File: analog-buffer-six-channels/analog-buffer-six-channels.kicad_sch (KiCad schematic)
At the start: 8 parts, among them J1 Conn_02x10_Odd_Even, J2 Conn_02x08_Odd_Even

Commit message: Generated gerber files for analog-buffer board
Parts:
- added R14: DNP, Resistor_SMD:R_0805_2012Metric, symbol Device:R_Small
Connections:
- net -VCC: now also R14.1
- net GND: now also R14.2
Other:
- note added: "[1]"
- note added: "[1] Place this resistor if single supply operation is intended. Please note that if this resistor is placed, -Vcc and GND will be shorted. Thus, it must be ensured that no active supply is present on the -Vcc rail."
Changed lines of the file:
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@@
+    (stroke (width 0) (type default) (color 0 0 0 0))
+  )
+  (wire (pts (xy 67.056 64.77) (xy 69.596 64.77))
     (stroke (width 0) (type default) (color 0 0 0 0))
   )
@@
     (stroke (width 0) (type default) (color 0 0 0 0))
   )
+  (wire (pts (xy 74.676 64.77) (xy 77.216 64.77))
+    (stroke (width 0) (type default) (color 0 0 0 0))
+  )
   (wire (pts (xy 187.579 24.892) (xy 189.484 24.892))
     (stroke (width 0) (type default) (color 0 0 0 0))
@@
   (wire (pts (xy 236.093 33.401) (xy 236.093 35.941))
     (stroke (width 0) (type default) (color 0 0 0 0))
+  )
+  (text "[1]" (at 70.485 69.977 0)
+    (effects (font (size 1.27 1.27)) (justify left bottom))
+  )
+  (text "[1] Place this resistor if single supply operation is \nintended. Please note that if this resistor is placed,\n-Vcc and GND will be shorted. Thus, it must be ensured \nthat no active  supply is present on the -Vcc rail. "
+    (at 25.654 120.65 0)
+    (effects (font (size 1.27 1.27)) (justify left bottom))
   )
   (label "S4o" (at 169.291 29.972 0)
@@
     )
     (property "Datasheet" "" (id 3) (at 248.793 41.275 0)
+      (effects (font (size 1.27 1.27)) hide)
+    )
+    (pin "1")
+  )
+  (symbol (lib_id "CL_power:-VCC") (at 67.056 64.77 0) (unit 1)
+    (in_bom yes) (on_board yes)
+    (property "Reference" "#PWR030" (id 0) (at 67.056 68.58 0)
+      (effects (font (size 1.27 1.27)) hide)
+    )
+    (property "Value" "-VCC" (id 1) (at 67.056 60.96 0))
+    (property "Footprint" "" (id 2) (at 67.056 64.77 0)
+      (effects (font (size 1.27 1.27)) hide)
+    )
+    (property "Datasheet" "" (id 3) (at 67.056 64.77 0)
       (effects (font (size 1.27 1.27)) hide)
     )
@@
     (pin "9")
   )
+  (symbol (lib_id "power:GND") (at 77.216 64.77 180) (unit 1)
+    (in_bom yes) (on_board yes)
+    (property "Reference" "#PWR031" (id 0) (at 77.216 58.42 0)
+      (effects (font (size 1.27 1.27)) hide)
+    )
+    (property "Value" "GND" (id 1) (at 77.216 60.96 0))
+    (property "Footprint" "" (id 2) (at 77.216 64.77 0)
+      (effects (font (size 1.27 1.27)) hide)
+    )
+    (property "Datasheet" "" (id 3) (at 77.216 64.77 0)
+      (effects (font (size 1.27 1.27)) hide)
+    )
+    (pin "1")
+  )
   (symbol (lib_id "CL_power:-VCC") (at 187.579 35.052 180) (unit 1)
     (in_bom yes) (on_board yes)
@@
     )
     (property "Datasheet" "~" (id 3) (at 94.361 29.591 0)
+      (effects (font (size 1.27 1.27)) hide)
+    )
+    (pin "1")
+    (pin "2")
+  )
+  (symbol (lib_id "Device:R_Small") (at 72.136 64.77 90) (unit 1)
+    (in_bom yes) (on_board yes)
+    (property "Reference" "R14" (id 0) (at 74.041 62.992 90)
+      (effects (font (size 1.27 1.27)) (justify left))
+    )
+    (property "Value" "DNP" (id 1) (at 74.168 66.548 90)
+      (effects (font (size 1.27 1.27)) (justify left))
+    )
+    (property "Footprint" "Resistor_SMD:R_0805_2012Metric" (id 2) (at 72.136 64.77 0)
+      (effects (font (size 1.27 1.27)) hide)
+    )
+    (property "Datasheet" "~" (id 3) (at 72.136 64.77 0)
       (effects (font (size 1.27 1.27)) hide)
     )
@@
       (reference "#PWR029") (unit 1) (value "GND") (footprint "")
     )
+    (path "/6df7937c-24c3-419f-af90-5ffeeccc6aa6"
+      (reference "#PWR030") (unit 1) (value "-VCC") (footprint "")
+    )
+    (path "/8576ff88-bd85-40e8-9199-0443b9c27d74"
+      (reference "#PWR031") (unit 1) (value "GND") (footprint "")
+    )
     (path "/5b3bbc6a-43cc-4842-9485-8d4a7c1538b8"
       (reference "C1") (unit 1) (value "10uF") (footprint "Capacitor_SMD:C_0805_2012Metric")
@@
       (reference "R13") (unit 1) (value "TBD") (footprint "Resistor_SMD:R_0805_2012Metric")
     )
+    (path "/a28eb529-2781-473b-a0cf-7bd7bdd12fbc"
+      (reference "R14") (unit 1) (value "DNP") (footprint "Resistor_SMD:R_0805_2012Metric")
+    )
     (path "/a3eeb221-bcc9-4595-85cc-dbb9e8280b98/05e6d6c6-a339-4aa3-92cf-09ecf6075749"

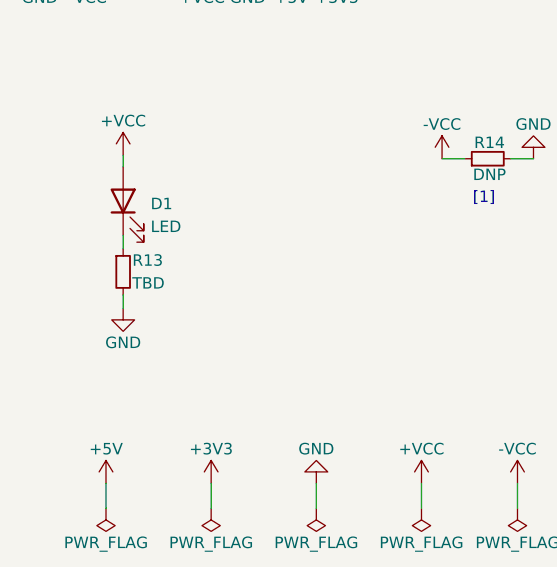
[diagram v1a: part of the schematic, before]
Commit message: Created bom for analog buffer board
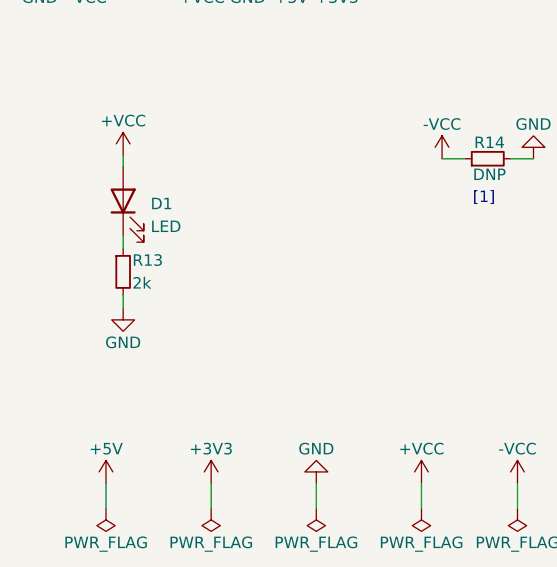
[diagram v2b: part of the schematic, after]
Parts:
- R13: value TBD -> 2k
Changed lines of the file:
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@@
       (effects (font (size 1.27 1.27)) (justify left))
     )
-    (property "Value" "TBD" (id 1) (at 32.639 78.613 0)
+    (property "Value" "2k" (id 1) (at 32.639 78.613 0)
       (effects (font (size 1.27 1.27)) (justify left))
     )
@@
     )
     (path "/7deeb18e-5967-4a76-b7ef-1bd5f0b0211c"
-      (reference "R13") (unit 1) (value "TBD") (footprint "Resistor_SMD:R_0805_2012Metric")
+      (reference "R13") (unit 1) (value "2k") (footprint "Resistor_SMD:R_0805_2012Metric")
     )
     (path "/a28eb529-2781-473b-a0cf-7bd7bdd12fbc"
